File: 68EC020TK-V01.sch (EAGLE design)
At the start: 100 parts, among them IC10 74HCT245PW, IC11 74HCT245PW, IC12 AM29F010S, IC13 XC95288XL-TQ144, IC14 ICS570B, IC15 74HCT245PW, IC2 MC68EC020RP, IC3 74ACT16245, IC4 74ACT16245, IC5 LD117AS33TR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

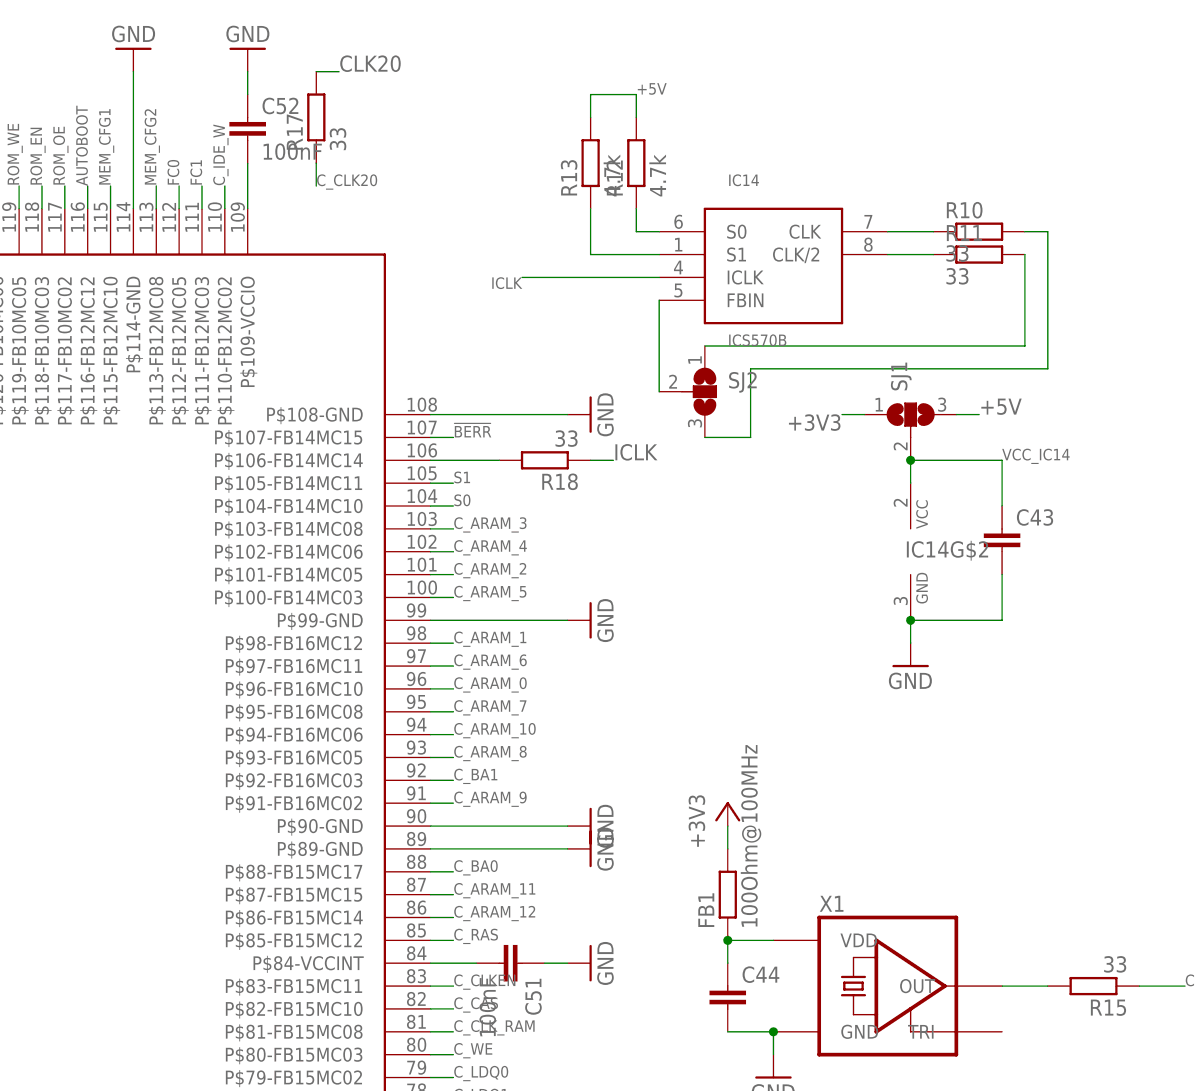
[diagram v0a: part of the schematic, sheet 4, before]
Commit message: bus & autoconfig OK IDE-RW-fix but IDE& mem not working
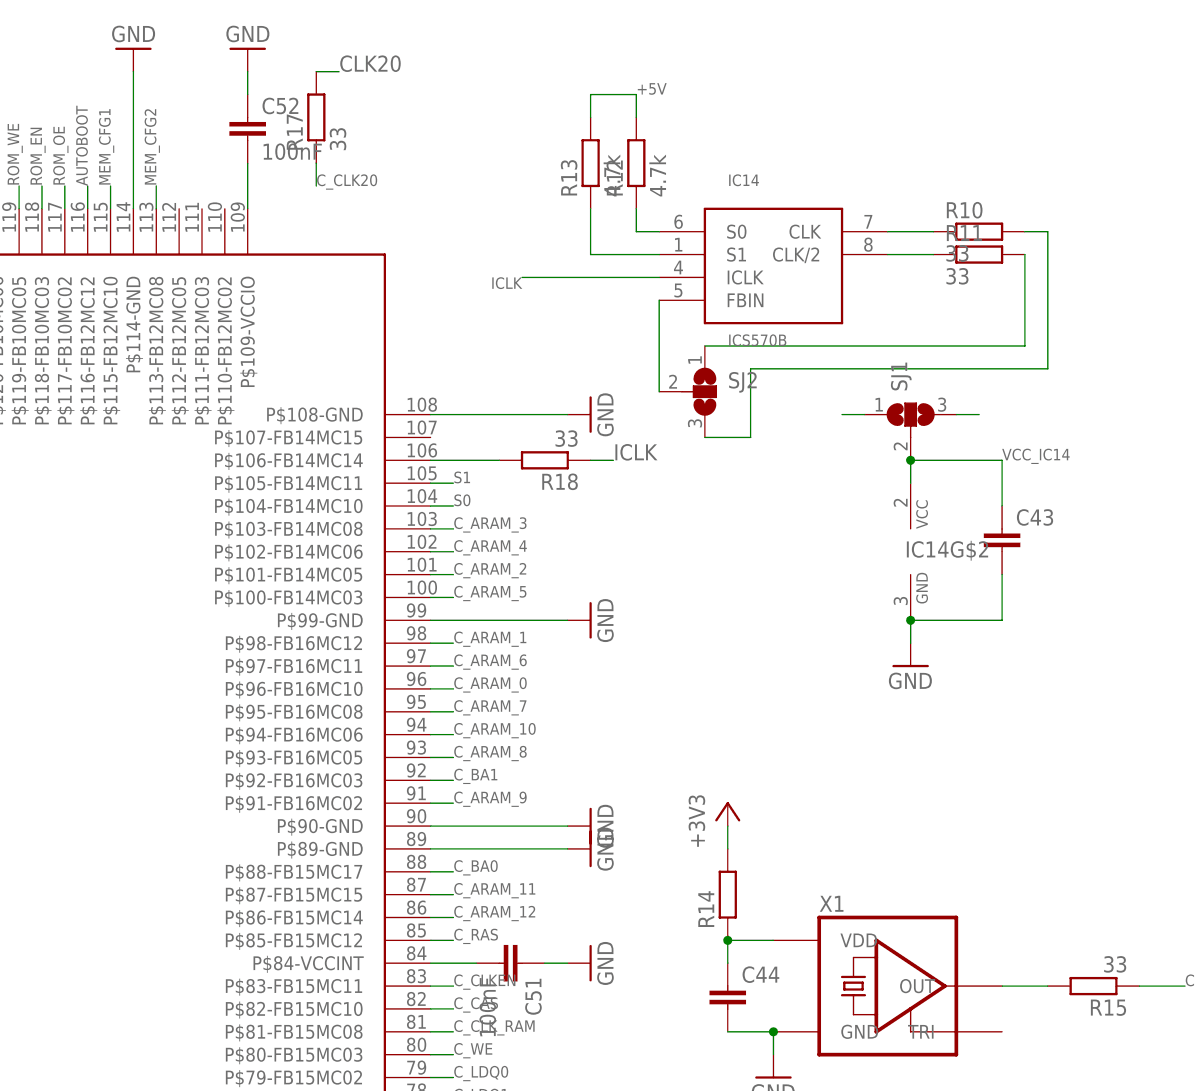
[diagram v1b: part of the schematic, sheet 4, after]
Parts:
- R14: value 100Ohm@100MHz -> (none)
- renumbered FB1 to R14
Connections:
- net !BERR: no longer IC13.P$107-FB14MC15
- net C_IDE_W: no longer IC13.P$110-FB12MC02
- net FC0: no longer IC13.P$112-FB12MC05
- net FC1: no longer IC13.P$111-FB12MC03
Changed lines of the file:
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@@
 <part name="GND39" library="supply1" deviceset="GND" device=""/>
 <part name="C44" library="rcl" deviceset="C-EU" device="C0603K"/>
-<part name="FB1" library="rcl" deviceset="R-EU_" device="R0603" value="100Ohm@100MHz"/>
+<part name="R14" library="rcl" deviceset="R-EU_" device="R0603"/>
 <part name="R15" library="rcl" deviceset="R-EU_" device="R0603" value="33"/>
 <part name="R17" library="rcl" deviceset="R-EU_" device="R0603" value="33"/>
@@
 </segment>
 </net>
+<net name="C_IDE_W" class="0">
+<segment>
+<pinref part="IC11" gate="A" pin="A2"/>
+<wire x1="22.86" y1="87.63" x2="20.32" y2="87.63" width="0.1524" layer="91"/>
+<label x="20.32" y="87.63" size="1.27" layer="95" rot="R180"/>
+</segment>
+</net>
+<net name="C_IDE_R" class="0">
+<segment>
+<pinref part="IC11" gate="A" pin="A3"/>
+<wire x1="22.86" y1="85.09" x2="20.32" y2="85.09" width="0.1524" layer="91"/>
+<label x="20.32" y="85.09" size="1.27" layer="95" rot="R180"/>
+</segment>
+</net>
 <net name="C_IDE_CS1" class="0">
 <segment>
@@
 </segment>
 </net>
-<net name="C_IDE_W" class="0">
-<segment>
-<pinref part="IC11" gate="A" pin="A2"/>
-<wire x1="22.86" y1="87.63" x2="20.32" y2="87.63" width="0.1524" layer="91"/>
-<label x="20.32" y="87.63" size="1.27" layer="95" rot="R180"/>
-</segment>
-</net>
-<net name="C_IDE_R" class="0">
-<segment>
-<pinref part="IC11" gate="A" pin="A3"/>
-<wire x1="22.86" y1="85.09" x2="20.32" y2="85.09" width="0.1524" layer="91"/>
-<label x="20.32" y="85.09" size="1.27" layer="95" rot="R180"/>
-</segment>
-</net>
 </nets>
 </sheet>
@@
 <instance part="GND39" gate="1" x="205.74" y="60.96"/>
 <instance part="C44" gate="G$1" x="200.66" y="71.12"/>
-<instance part="FB1" gate="G$1" x="200.66" y="81.28" rot="R90"/>
+<instance part="R14" gate="G$1" x="200.66" y="81.28" rot="R90"/>
 <instance part="R15" gate="G$1" x="241.3" y="71.12" rot="R180"/>
 <instance part="R17" gate="G$1" x="154.94" y="167.64" rot="R90"/>
@@
 <pinref part="SJ1" gate="G$1" pin="3"/>
 <wire x1="226.06" y1="134.62" x2="228.6" y2="134.62" width="0.1524" layer="91"/>
-<label x="228.6" y="134.62" size="1.778" layer="95"/>
 </segment>
 <segment>
@@
 <segment>
 <pinref part="+3V12" gate="G$1" pin="+3V3"/>
-<pinref part="FB1" gate="G$1" pin="2"/>
+<pinref part="R14" gate="G$1" pin="2"/>
 <wire x1="200.66" y1="86.36" x2="200.66" y2="88.9" width="0.1524" layer="91"/>
 </segment>
@@
 <pinref part="SJ1" gate="G$1" pin="1"/>
 <wire x1="215.9" y1="134.62" x2="213.36" y2="134.62" width="0.1524" layer="91"/>
-<label x="213.36" y="134.62" size="1.778" layer="95" rot="R180"/>
 </segment>
 </net>
@@
 <wire x1="205.74" y1="76.2" x2="200.66" y2="76.2" width="0.1524" layer="91"/>
 <wire x1="200.66" y1="76.2" x2="200.66" y2="73.66" width="0.1524" layer="91"/>
-<pinref part="FB1" gate="G$1" pin="1"/>
+<pinref part="R14" gate="G$1" pin="1"/>
 <junction x="200.66" y="76.2"/>
 </segment>
@@
 </segment>
 </net>
-<net name="FC0" class="0">
-<segment>
-<pinref part="IC13" gate="G$1" pin="P$112-FB12MC05"/>
-<wire x1="139.7" y1="157.48" x2="139.7" y2="160.02" width="0.1524" layer="91"/>
-<label x="139.7" y="160.02" size="1.27" layer="95" rot="R90"/>
-</segment>
-</net>
-<net name="FC1" class="0">
-<segment>
-<pinref part="IC13" gate="G$1" pin="P$111-FB12MC03"/>
-<wire x1="142.24" y1="157.48" x2="142.24" y2="160.02" width="0.1524" layer="91"/>
-<label x="142.24" y="160.02" size="1.27" layer="95" rot="R90"/>
-</segment>
-</net>
-<net name="!BERR" class="0">
-<segment>
-<pinref part="IC13" gate="G$1" pin="P$107-FB14MC15"/>
-<wire x1="167.64" y1="132.08" x2="170.18" y2="132.08" width="0.1524" layer="91"/>
-<label x="170.18" y="132.08" size="1.27" layer="95"/>
-</segment>
-</net>
-<net name="C_IDE_W" class="0">
-<segment>
-<pinref part="IC13" gate="G$1" pin="P$110-FB12MC02"/>
-<wire x1="144.78" y1="157.48" x2="144.78" y2="160.02" width="0.1524" layer="91"/>
-<label x="144.78" y="160.02" size="1.27" layer="95" rot="R90"/>
-</segment>
-</net>
